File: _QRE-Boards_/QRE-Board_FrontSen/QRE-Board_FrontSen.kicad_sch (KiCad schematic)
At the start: 11 parts, among them J1 Conn_01x04_Pin, U1 QRE1113GR, U2 QRE1113GR

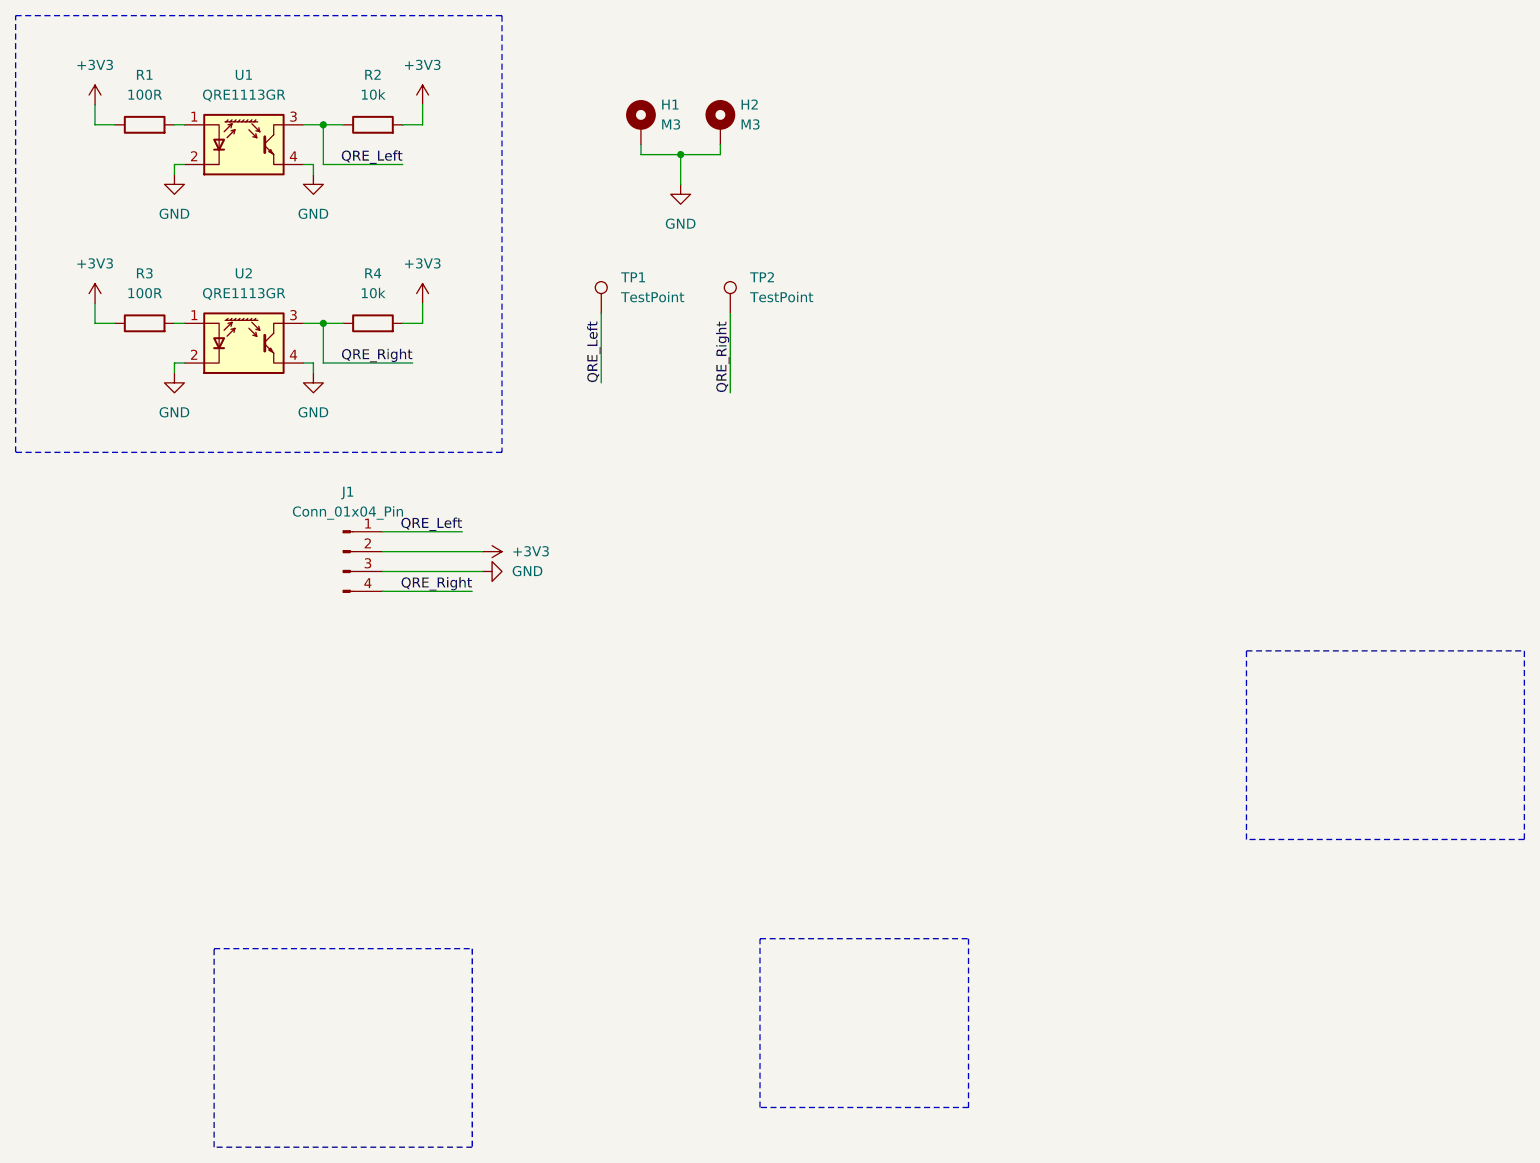
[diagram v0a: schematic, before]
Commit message: Remove junk and regesign QRE-Boards
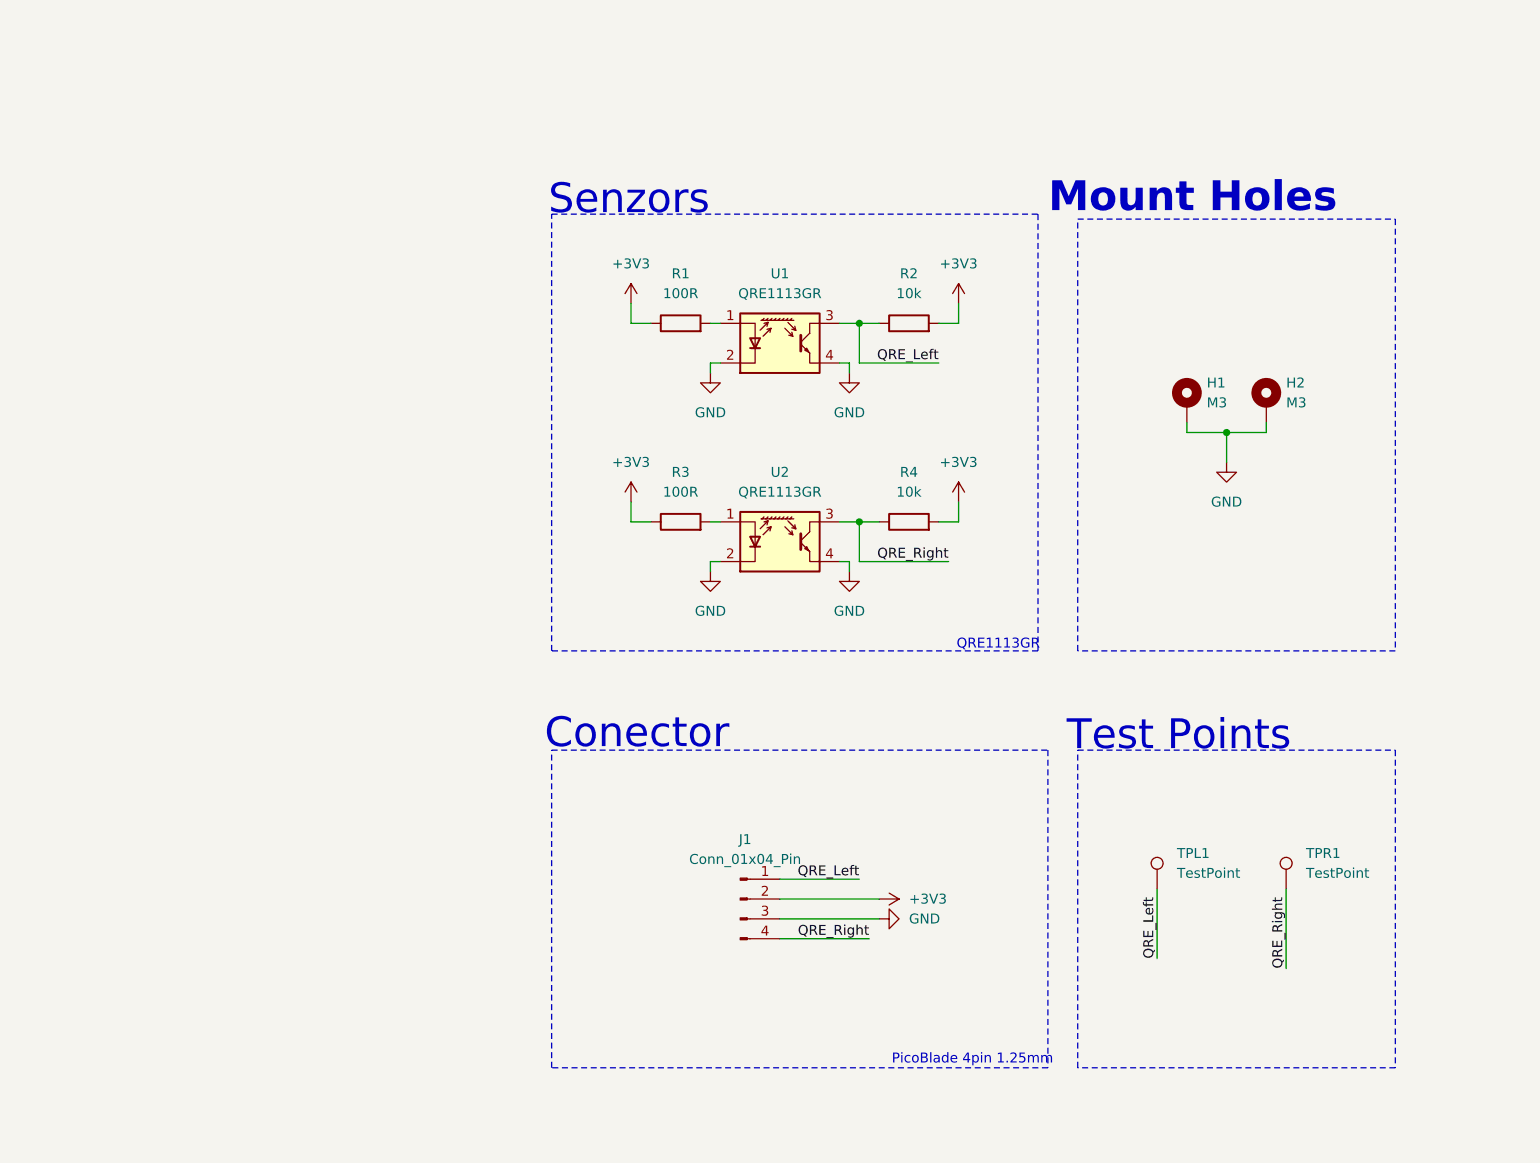
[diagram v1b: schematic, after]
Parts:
- renumbered TP1 to TPL1, TP2 to TPR1
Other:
- note added: "Conector"
- note added: "Mount Holes"
- note added: "PicoBlade 4pin 1.25mm"
- note added: "QRE1113GR"
- note added: "Senzors"
- note added: "Test Points"
- company: RoboCrew - Prosek -> Maded by Vadim Sobčuk
- title: Front Senzors rig for MiniSumo -> Front Senzors rig for MiniSumo robot
- moved on the sheet: H1, H2, J1, R1, R2, R3, R4, TPL1, TPR1, U1, U2
